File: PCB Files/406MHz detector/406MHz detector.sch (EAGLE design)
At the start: 18 parts, among them J1 switch

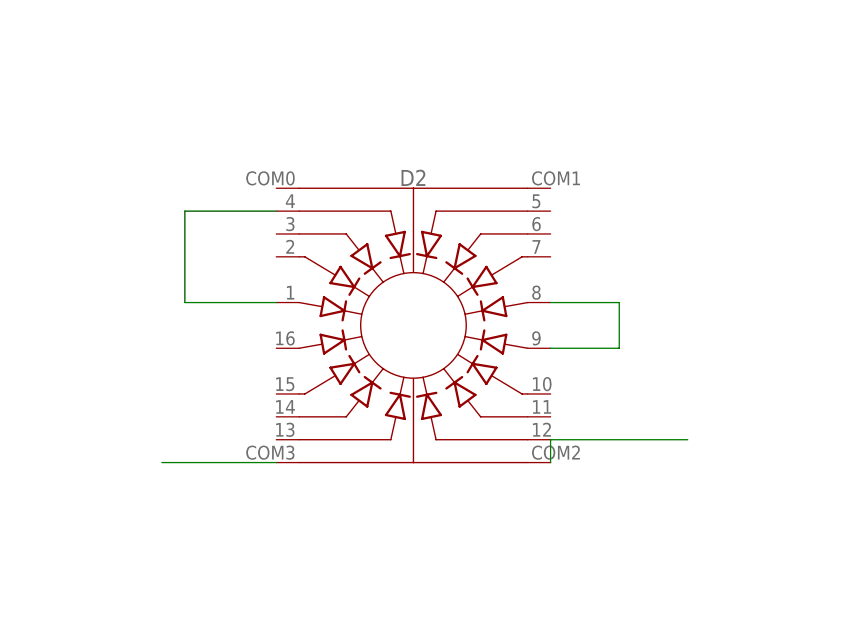
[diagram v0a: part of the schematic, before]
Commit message: removed sample led changes
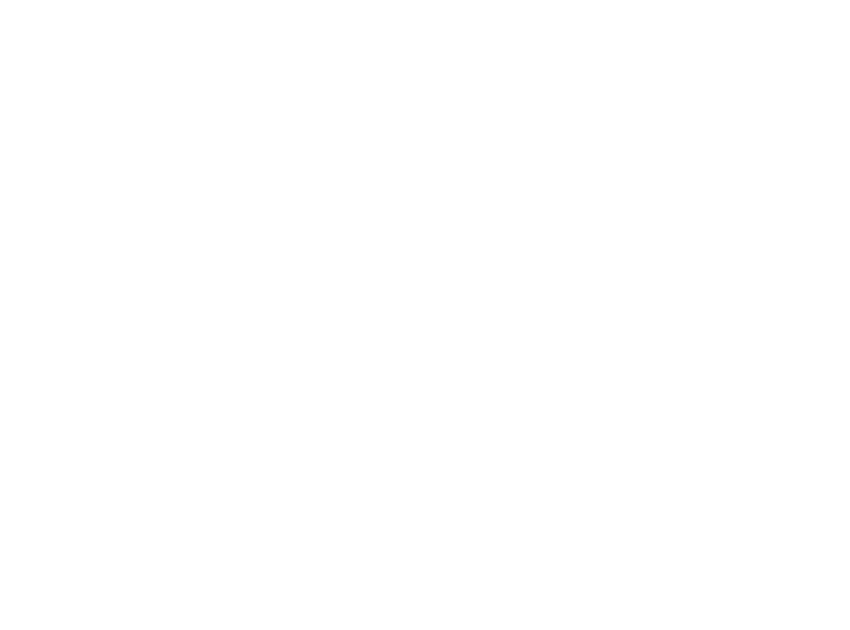
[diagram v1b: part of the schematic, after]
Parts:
- removed D2: (no value), SparkFun-LED:LED_RING
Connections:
- removed net N$15: D2.1, D2.4
- removed net N$16: D2.8, D2.9
- removed net N$17: D2.12, D2.COM2
- removed net N$18: D2.COM3
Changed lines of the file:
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@@
 <part name="GND6" library="SparkFun-PowerSymbols" library_urn="urn:adsk.eagle:library:530" deviceset="GND2" device="" value="GND"/>
 <part name="GND7" library="SparkFun-PowerSymbols" library_urn="urn:adsk.eagle:library:530" deviceset="GND2" device="" value="GND"/>
-<part name="D2" library="SparkFun-LED" library_urn="urn:adsk.eagle:library:529" deviceset="LED_RING" device="" package3d_urn="urn:adsk.eagle:package:39360/1"/>
 </parts>
 <sheets>
@@
 <attribute name="VALUE" x="119.38" y="92.202" size="1.778" layer="96" align="top-center"/>
 </instance>
-<instance part="D2" gate="G$1" x="193.04" y="96.52" smashed="yes">
-<attribute name="VALUE" x="193.04" y="81.026" size="1.778" layer="96" font="vector" align="top-center"/>
-<attribute name="NAME" x="193.04" y="112.014" size="1.778" layer="95" font="vector" align="bottom-center"/>
-</instance>
 </instances>
 <busses>
@@
 </segment>
 </net>
-<net name="N$15" class="0">
-<segment>
-<pinref part="D2" gate="G$1" pin="1"/>
-<wire x1="177.8" y1="99.06" x2="167.64" y2="99.06" width="0.1524" layer="91"/>
-<wire x1="167.64" y1="99.06" x2="167.64" y2="109.22" width="0.1524" layer="91"/>
-<pinref part="D2" gate="G$1" pin="4"/>
-<wire x1="167.64" y1="109.22" x2="177.8" y2="109.22" width="0.1524" layer="91"/>
-</segment>
-</net>
-<net name="N$16" class="0">
-<segment>
-<pinref part="D2" gate="G$1" pin="9"/>
-<wire x1="208.28" y1="93.98" x2="215.9" y2="93.98" width="0.1524" layer="91"/>
-<pinref part="D2" gate="G$1" pin="8"/>
-<wire x1="215.9" y1="93.98" x2="215.9" y2="99.06" width="0.1524" layer="91"/>
-<wire x1="215.9" y1="99.06" x2="208.28" y2="99.06" width="0.1524" layer="91"/>
-</segment>
-</net>
-<net name="N$17" class="0">
-<segment>
-<pinref part="D2" gate="G$1" pin="12"/>
-<pinref part="D2" gate="G$1" pin="COM2"/>
-<wire x1="223.52" y1="83.82" x2="208.28" y2="83.82" width="0.1524" layer="91"/>
-<wire x1="208.28" y1="83.82" x2="208.28" y2="81.28" width="0.1524" layer="91"/>
-</segment>
-</net>
-<net name="N$18" class="0">
-<segment>
-<pinref part="D2" gate="G$1" pin="COM3"/>
-<wire x1="177.8" y1="81.28" x2="165.1" y2="81.28" width="0.1524" layer="91"/>
-</segment>
-</net>

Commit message: added boxes and labels to schematic for separating workspaces
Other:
- note added: "CONNOR"
- note added: "NATHAN"
- note added: "SARAH"
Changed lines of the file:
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@@
 <wire x1="1524" y1="381" x2="1524" y2="0" width="0.1524" layer="150"/>
 <wire x1="1524" y1="0" x2="1016" y2="0" width="0.1524" layer="150"/>
+<text x="15.24" y="358.14" size="12.9032" layer="97">CONNOR</text>
+<text x="523.24" y="358.14" size="12.9032" layer="97">NATHAN</text>
+<text x="1028.7" y="358.14" size="12.9032" layer="97">SARAH</text>
 </plain>
 <instances>

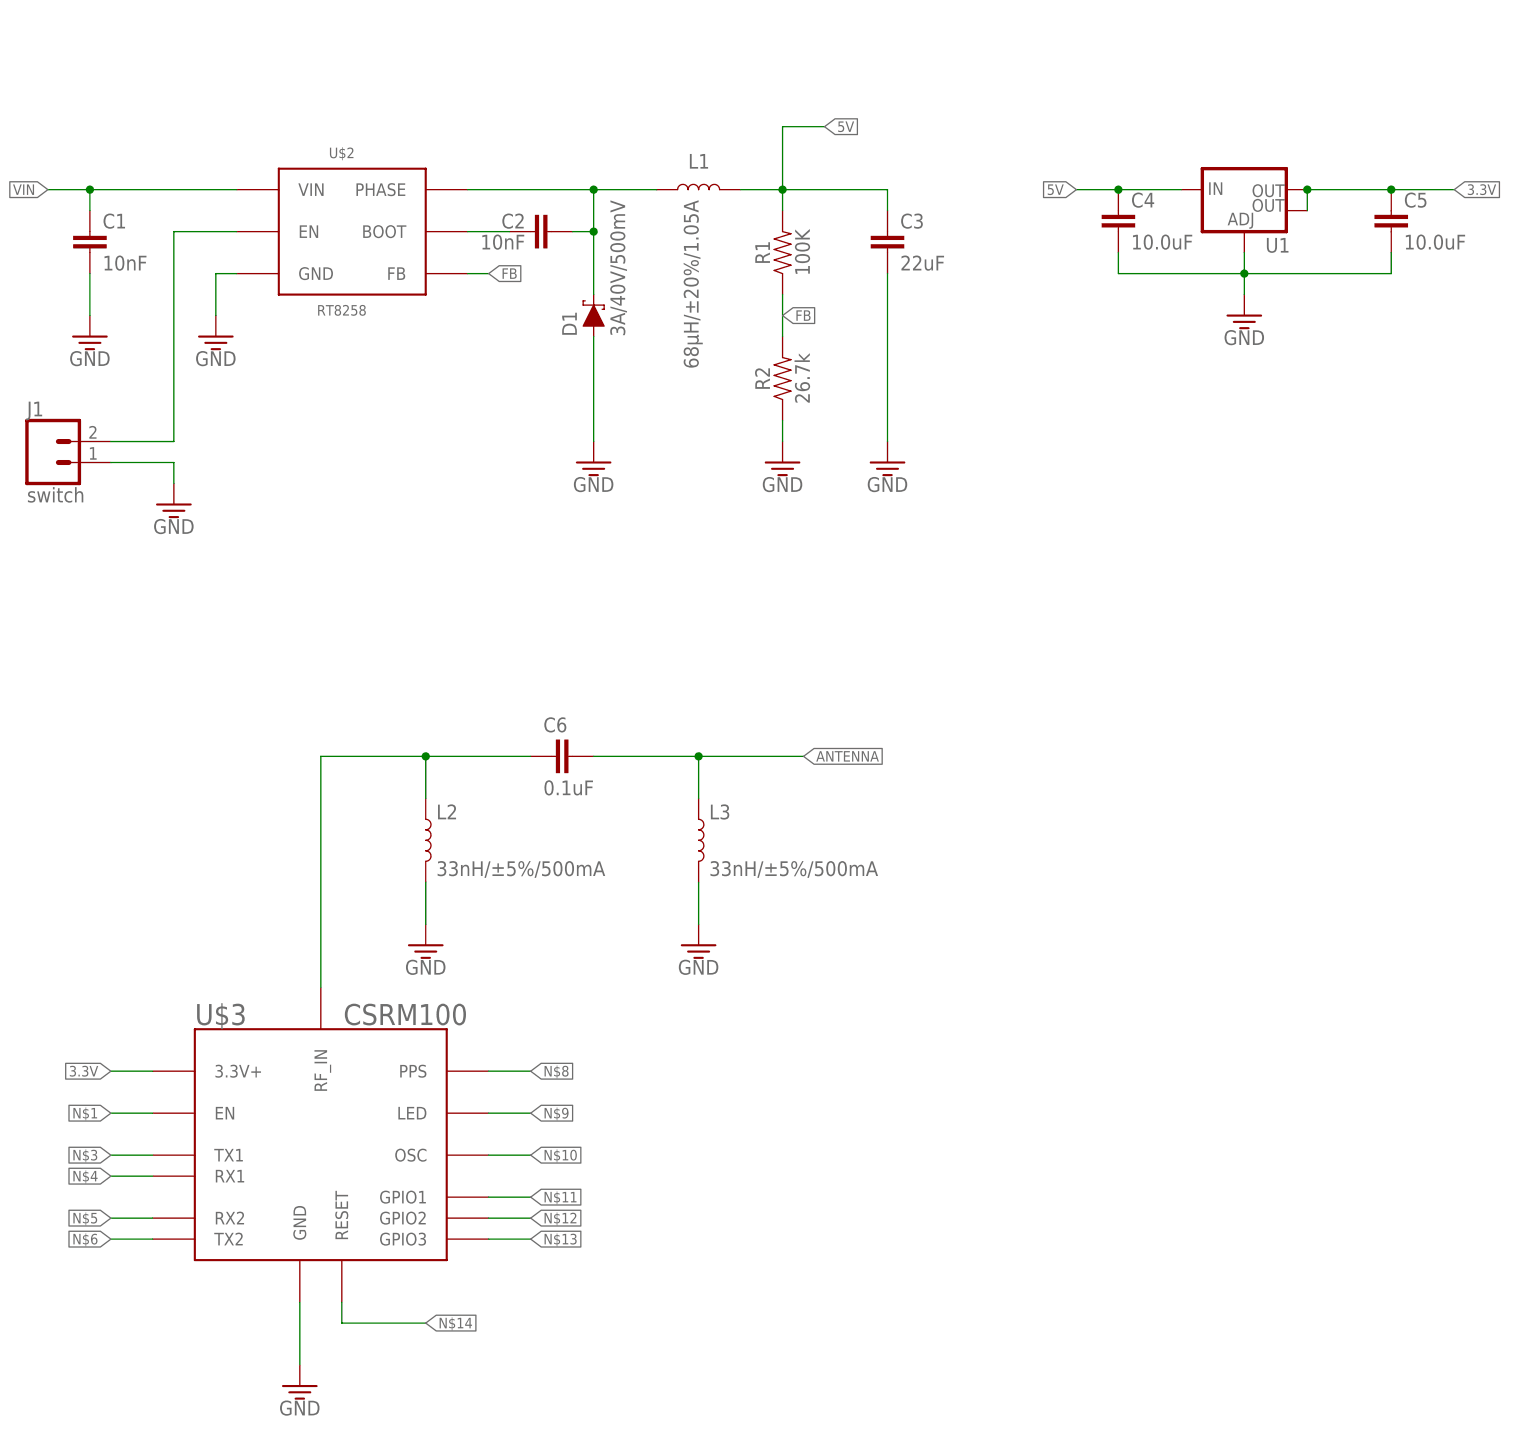
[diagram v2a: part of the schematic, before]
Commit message: removed problem with ground labels connecting to 3.3V net
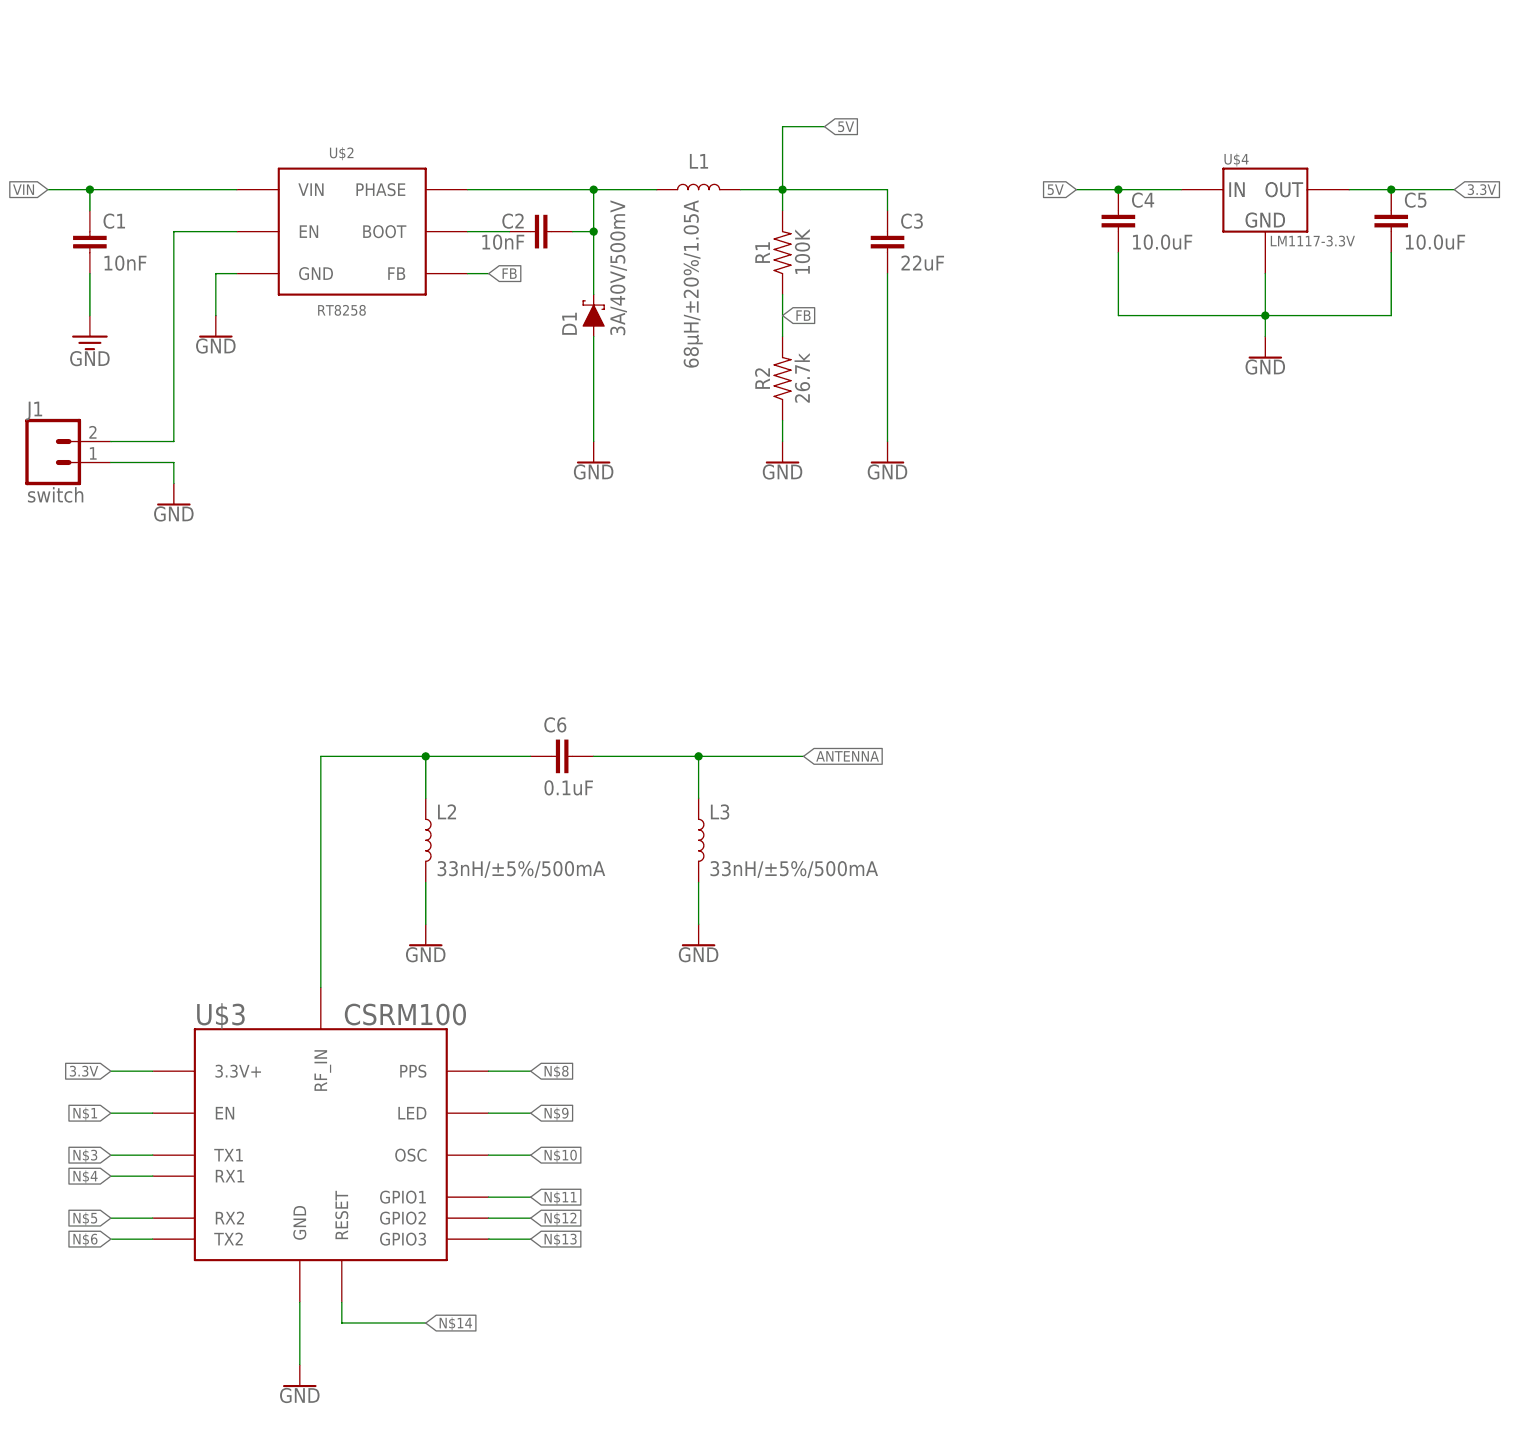
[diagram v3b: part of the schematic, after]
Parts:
- removed U1: (no value), SparkFun-IC-Power:V_REG_LM1117SOT223
- added U$4: LM1117-3.3V, capstone:LM1117-3.3V
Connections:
- net 3.3V: now also U$4.VOUT; no longer U1.OUT, U1.OUT@1
- net 5V: now also U$4.VIN; no longer U1.IN
- net GND: now also U$4.GND; no longer U1.ADJ

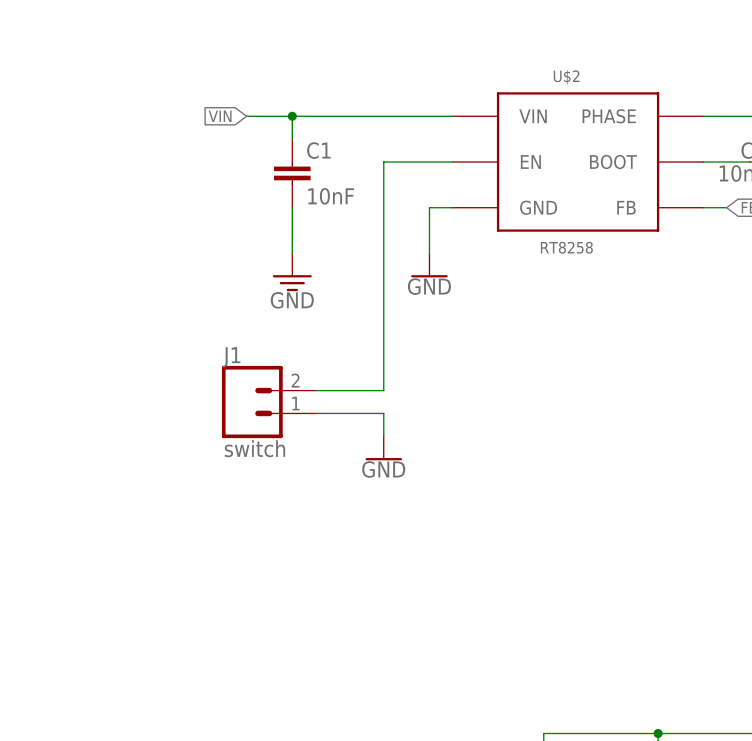
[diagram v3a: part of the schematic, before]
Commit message: added capactior to sw_reg enable input
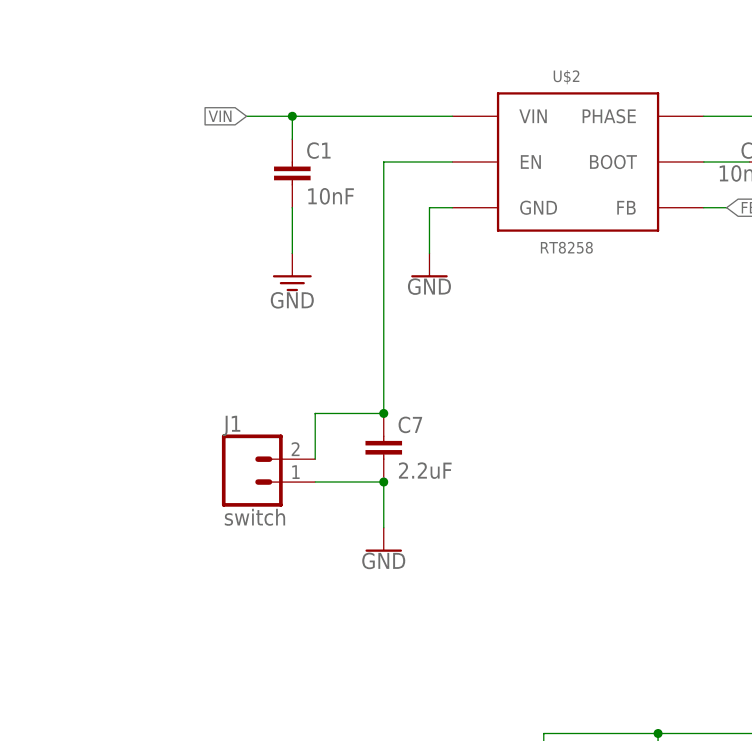
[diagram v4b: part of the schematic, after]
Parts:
- added C7: 2.2uF, SparkFun-Capacitors:2.2UF-0805-25V-(+80/-20%)
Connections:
- net GND: now also C7.2
- net N$2: now also C7.1
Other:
- moved on the sheet: J1
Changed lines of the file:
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@@
 <part name="GND6" library="SparkFun-PowerSymbols" library_urn="urn:adsk.eagle:library:530" deviceset="GND" device=""/>
 <part name="GND7" library="SparkFun-PowerSymbols" library_urn="urn:adsk.eagle:library:530" deviceset="GND" device=""/>
+<part name="C7" library="SparkFun-Capacitors" library_urn="urn:adsk.eagle:library:510" deviceset="2.2UF" device="-0805-25V-(+80/-20%)" package3d_urn="urn:adsk.eagle:package:37429/1" value="2.2uF"/>
 </parts>
 <sheets>
@@
 <attribute name="VALUE" x="45.72" y="165.862" size="1.778" layer="96" align="top-center"/>
 </instance>
-<instance part="J1" gate="G$1" x="40.64" y="152.4" smashed="yes">
-<attribute name="VALUE" x="38.1" y="147.574" size="1.778" layer="96" font="vector"/>
-<attribute name="NAME" x="38.1" y="157.988" size="1.778" layer="95" font="vector"/>
+<instance part="J1" gate="G$1" x="40.64" y="144.78" smashed="yes">
+<attribute name="VALUE" x="38.1" y="139.954" size="1.778" layer="96" font="vector"/>
+<attribute name="NAME" x="38.1" y="150.368" size="1.778" layer="95" font="vector"/>
 </instance>
 <instance part="D1" gate="G$1" x="106.68" y="170.18" smashed="yes" rot="R90">
@@
 <attribute name="VALUE" x="188.468" y="179.832" size="1.27" layer="96" align="top-left"/>
 </instance>
-<instance part="GND1" gate="1" x="55.88" y="147.32" smashed="yes">
-<attribute name="VALUE" x="55.88" y="147.066" size="1.778" layer="96" align="top-center"/>
+<instance part="GND1" gate="1" x="55.88" y="137.16" smashed="yes">
+<attribute name="VALUE" x="55.88" y="136.906" size="1.778" layer="96" align="top-center"/>
 </instance>
 <instance part="GND2" gate="1" x="106.68" y="152.4" smashed="yes">
@@
 <instance part="GND7" gate="1" x="119.38" y="93.98" smashed="yes">
 <attribute name="VALUE" x="119.38" y="93.726" size="1.778" layer="96" align="top-center"/>
+</instance>
+<instance part="C7" gate="G$1" x="55.88" y="147.32" smashed="yes">
+<attribute name="NAME" x="57.404" y="150.241" size="1.778" layer="95" font="vector"/>
+<attribute name="VALUE" x="57.404" y="145.161" size="1.778" layer="96" font="vector"/>
 </instance>
 </instances>
@@
 <segment>
 <pinref part="J1" gate="G$1" pin="2"/>
-<wire x1="48.26" y1="154.94" x2="55.88" y2="154.94" width="0.1524" layer="91"/>
-<wire x1="55.88" y1="154.94" x2="55.88" y2="180.34" width="0.1524" layer="91"/>
+<wire x1="48.26" y1="147.32" x2="48.26" y2="152.4" width="0.1524" layer="91"/>
+<wire x1="48.26" y1="152.4" x2="55.88" y2="152.4" width="0.1524" layer="91"/>
+<wire x1="55.88" y1="152.4" x2="55.88" y2="180.34" width="0.1524" layer="91"/>
 <pinref part="U$2" gate="G$1" pin="EN"/>
 <wire x1="55.88" y1="180.34" x2="63.5" y2="180.34" width="0.1524" layer="91"/>
+<pinref part="C7" gate="G$1" pin="1"/>
+<junction x="55.88" y="152.4"/>
 </segment>
 </net>
@@
 <segment>
 <pinref part="J1" gate="G$1" pin="1"/>
-<wire x1="55.88" y1="149.86" x2="55.88" y2="152.4" width="0.1524" layer="91"/>
-<wire x1="55.88" y1="152.4" x2="48.26" y2="152.4" width="0.1524" layer="91"/>
+<wire x1="55.88" y1="139.7" x2="55.88" y2="144.78" width="0.1524" layer="91"/>
+<wire x1="55.88" y1="144.78" x2="48.26" y2="144.78" width="0.1524" layer="91"/>
 <pinref part="GND1" gate="1" pin="GND"/>
-</segment>
-<segment>
+<pinref part="C7" gate="G$1" pin="2"/>
+<junction x="55.88" y="144.78"/>
+</segment>
+<segment>
